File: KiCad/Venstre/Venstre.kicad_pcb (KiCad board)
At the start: 2 copper layers, 16 parts, among them Q1 NMOS_IRL530, Q3 NMOS_IRL530, Q5 NMOS_IRL530

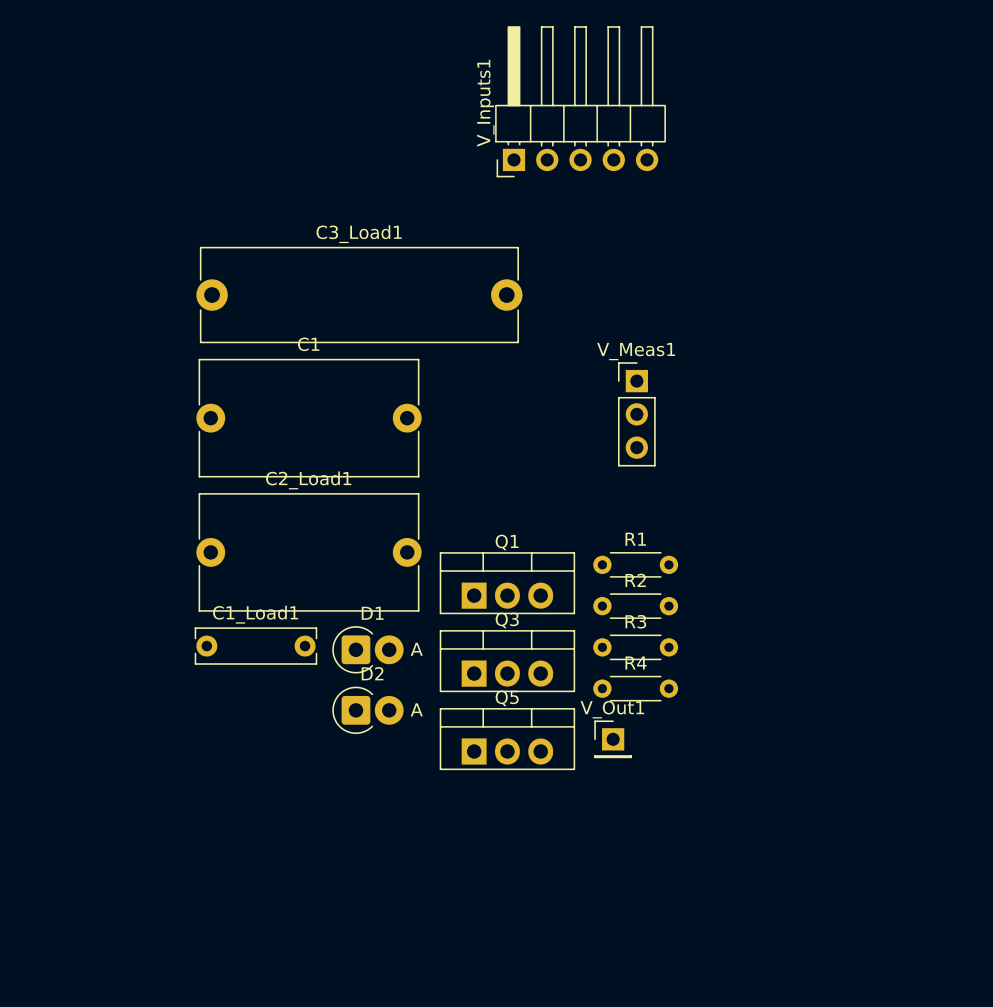
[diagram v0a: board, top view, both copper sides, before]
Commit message: Venstre og Højre pcb klar til produktion
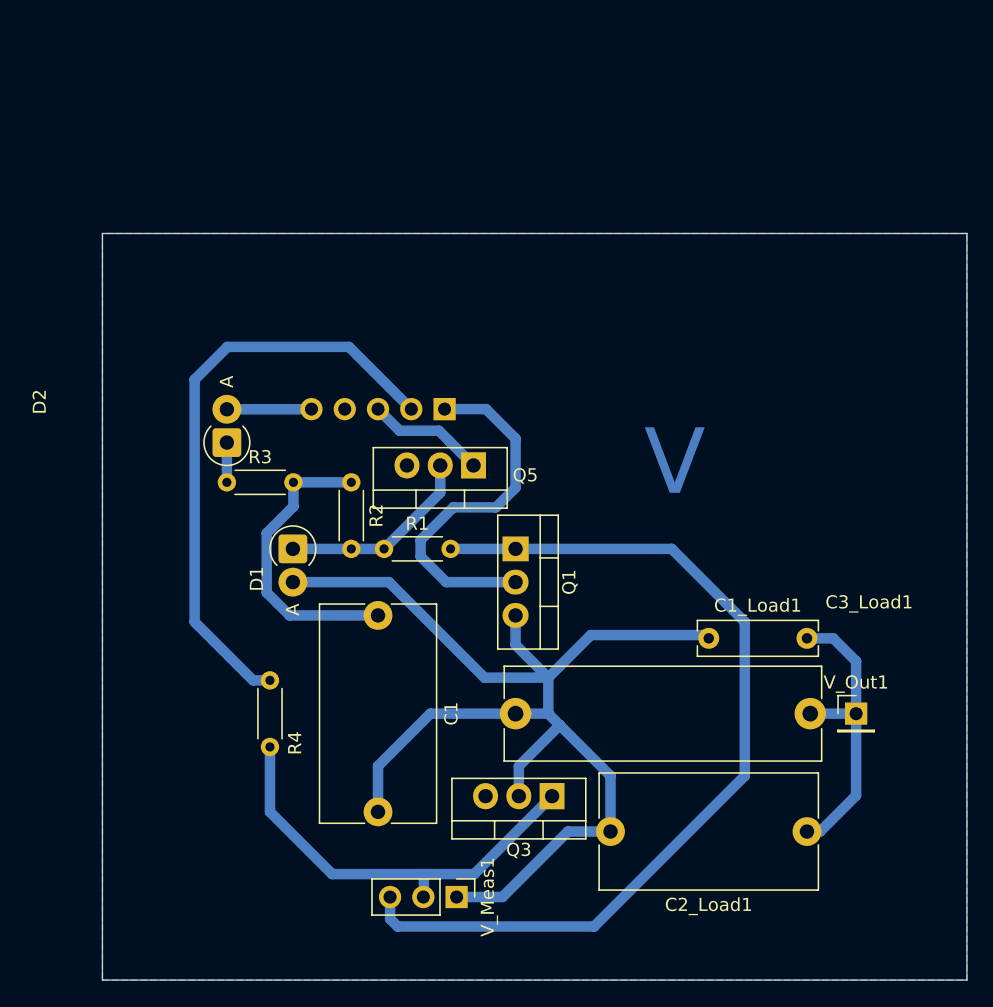
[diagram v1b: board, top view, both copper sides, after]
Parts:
- V_Inputs1: moved to B.Cu
- moved C2_Load1 50.3 mm to (171.0, 109.9), turned to 180 degrees
- moved V_Meas1 41.7 mm to (144.3, 114.9), turned to -90 degrees
- moved C3_Load1 39.5 mm to (148.8, 100.9)
- moved C1_Load1 38.3 mm to (163.5, 95.2)
- moved R3 31.3 mm to (126.8, 83.2)
- moved R4 25.4 mm to (130.0, 98.4), turned to -90 degrees
- moved D2 22.7 mm to (126.8, 80.2), turned to 90 degrees
- moved Q5 21.8 mm to (145.6, 82.0), turned to 180 degrees
- moved R2 21.4 mm to (136.2, 83.2), turned to -90 degrees
- moved V_Inputs1 19.7 mm to (143.4, 77.7)
- moved C1 19.7 mm to (138.3, 93.4), turned to -90 degrees
- moved V_Out1 18.7 mm to (174.8, 100.9)
- moved R1 16.7 mm to (138.8, 88.3)
- moved Q3 11.1 mm to (151.6, 107.2), turned to 180 degrees
- moved D1 9.09 mm to (131.8, 88.3), turned to -90 degrees
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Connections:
- Q1 pad 1: +9V -> /Meas_GATE_M1
- Q1 pad 2: /Meas_GATE_M1 -> +9V
- Q3 pad 1: /Meas_V_Out -> /Meas_GATE_M3
- Q3 pad 2: /Meas_GATE_M3 -> /Meas_V_Out
- Q5 pad 1: Net-(D1-K) -> /PWM2_NOT
- Q5 pad 2: /PWM2_NOT -> Net-(D1-K)
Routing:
- net /Meas_V_Out: track 0.00 -> 94.8 mm
- net /Meas_GATE_M1: track 0.00 -> 70.3 mm
- net /PWM1: track 0.00 -> 45.6 mm
- net /Meas_GATE_M3: track 0.00 -> 32.8 mm
- net +9V: track 0.00 -> 28.3 mm
- net Net-(V_Out1-Pin_1): track 0.00 -> 23.1 mm
- net Net-(C1-Pad1): track 0.00 -> 22.9 mm
- net Net-(D1-K): track 0.00 -> 15.1 mm
- net /PWM2_NOT: track 0.00 -> 9.08 mm
- net +5V: track 0.00 -> 6.47 mm
- net Net-(D2-K): track 0.00 -> 3.04 mm
- added copper zone on B.Cu, net GND
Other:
- board outline added: 66 x 57 mm
- board text added: "V"
